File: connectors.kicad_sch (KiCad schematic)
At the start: 3 parts, among them J7 Pads for coax, J8 Relay control, J9 BNC

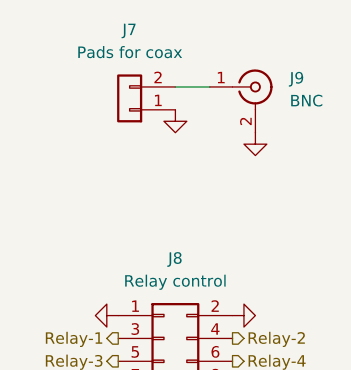
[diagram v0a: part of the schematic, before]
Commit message: changed to 1 to 6
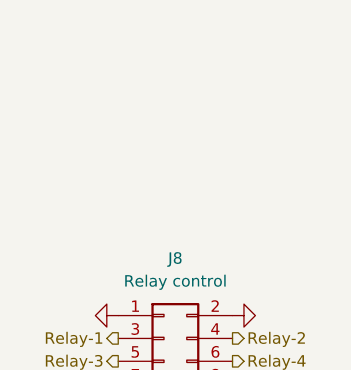
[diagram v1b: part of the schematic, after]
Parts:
- removed J7: Pads for coax, Connector_PinHeader_2.54mm:PinHeader_1x02_P2.54mm_Vertical, symbol Components:Conn_01x02
- removed J9: BNC, Components:BNC_vertical, symbol Components:BNC
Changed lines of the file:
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@@
 (kicad_sch (version 20211123) (generator eeschema)
   (paper "A4")
-  (wire (pts (xy 139.7 74.93) (xy 143.51 74.93))
-    (stroke (width 0) (type default) (color 0 0 0 0))
-  )
   (hierarchical_label "Relay-5" (shape output) (at 133.35 107.95 180)
     (effects (font (size 1.27 1.27)) (justify right))
@@
   (symbol (lib_id "power:GND") (at 146.05 100.33 90) (unit 1)
     (in_bom yes) (on_board yes) (fields_autoplaced)
-    (property "Reference" "#PWR046" (id 0) (at 152.4 100.33 0)
+    (property "Reference" "#PWR040" (id 0) (at 152.4 100.33 0)
       (effects (font (size 1.27 1.27)) hide)
     )
@@
   (symbol (lib_id "power:GND") (at 133.35 100.33 270) (mirror x) (unit 1)
     (in_bom yes) (on_board yes) (fields_autoplaced)
-    (property "Reference" "#PWR044" (id 0) (at 127 100.33 0)
+    (property "Reference" "#PWR039" (id 0) (at 127 100.33 0)
       (effects (font (size 1.27 1.27)) hide)
     )
@@
     (pin "8")
   )
-  (symbol (lib_id "Components:BNC") (at 148.59 74.93 0) (unit 1)
-    (in_bom yes) (on_board yes) (fields_autoplaced)
-    (property "Reference" "J9" (id 0) (at 152.4 73.9531 0)
-      (effects (font (size 1.27 1.27)) (justify left))
-    )
-    (property "Value" "BNC" (id 1) (at 152.4 76.4931 0)
-      (effects (font (size 1.27 1.27)) (justify left))
-    )
-    (property "Footprint" "Components:BNC_vertical" (id 2) (at 148.59 74.93 0)
-      (effects (font (size 1.27 1.27)) hide)
-    )
-    (property "Datasheet" " ~" (id 3) (at 148.59 74.93 0)
-      (effects (font (size 1.27 1.27)) hide)
-    )
-    (pin "1")
-    (pin "2")
-  )
-  (symbol (lib_id "Components:Conn_01x02") (at 134.62 77.47 180) (unit 1)
-    (in_bom yes) (on_board yes) (fields_autoplaced)
-    (property "Reference" "J7" (id 0) (at 134.62 68.58 0))
-    (property "Value" "Pads for coax" (id 1) (at 134.62 71.12 0))
-    (property "Footprint" "Connector_PinHeader_2.54mm:PinHeader_1x02_P2.54mm_Vertical" (id 2) (at 134.62 77.47 0)
-      (effects (font (size 1.27 1.27)) hide)
-    )
-    (property "Datasheet" "~" (id 3) (at 134.62 77.47 0)
-      (effects (font (size 1.27 1.27)) hide)
-    )
-    (pin "1")
-    (pin "2")
-  )
-  (symbol (lib_id "power:GND") (at 139.7 77.47 0) (unit 1)
-    (in_bom yes) (on_board yes) (fields_autoplaced)
-    (property "Reference" "#PWR045" (id 0) (at 139.7 83.82 0)
-      (effects (font (size 1.27 1.27)) hide)
-    )
-    (property "Value" "GND" (id 1) (at 139.7 82.55 0)
-      (effects (font (size 1.27 1.27)) hide)
-    )
-    (property "Footprint" "" (id 2) (at 139.7 77.47 0)
-      (effects (font (size 1.27 1.27)) hide)
-    )
-    (property "Datasheet" "" (id 3) (at 139.7 77.47 0)
-      (effects (font (size 1.27 1.27)) hide)
-    )
-    (pin "1")
-  )
-  (symbol (lib_id "power:GND") (at 148.59 80.01 0) (unit 1)
-    (in_bom yes) (on_board yes) (fields_autoplaced)
-    (property "Reference" "#PWR047" (id 0) (at 148.59 86.36 0)
-      (effects (font (size 1.27 1.27)) hide)
-    )
-    (property "Value" "GND" (id 1) (at 148.59 85.09 0)
-      (effects (font (size 1.27 1.27)) hide)
-    )
-    (property "Footprint" "" (id 2) (at 148.59 80.01 0)
-      (effects (font (size 1.27 1.27)) hide)
-    )
-    (property "Datasheet" "" (id 3) (at 148.59 80.01 0)
-      (effects (font (size 1.27 1.27)) hide)
-    )
-    (pin "1")
-  )
 )

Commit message: pcb routed and made gerbers
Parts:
- added J1: RF Conn, Components:PinHeader_2x06_P2.54mm_Horizontal, symbol Connector_Generic:Conn_02x06_Odd_Even
- renumbered J8 to J3
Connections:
- net GND: now also J1.10 (Pin_10), J1.12 (Pin_12), J1.2 (Pin_2), J1.4 (Pin_4), J1.6 (Pin_6), J1.8 (Pin_8); no longer J3.2 (Pin_2)
- net Relay-2: now also J3.5 (Pin_5); no longer J3.4 (Pin_4)
- net Relay-3: now also J3.7 (Pin_7); no longer J3.5 (Pin_5)
- net Relay-4: now also J3.8 (Pin_8); no longer J3.6 (Pin_6)
- net Relay-5: now also J3.6 (Pin_6); no longer J3.7 (Pin_7)
- net Relay-6: now also J3.4 (Pin_4); no longer J3.8 (Pin_8)
- new net +12V: J3.2 (Pin_2)
- new net RF-1: J1.1 (Pin_1)
- new net RF-2: J1.3 (Pin_3)
- new net RF-3: J1.5 (Pin_5)
- new net RF-4: J1.7 (Pin_7)
- new net RF-5: J1.9 (Pin_9)
- new net RF-6: J1.11 (Pin_11)
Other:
- note added: "2600 mils space between two j1 650 mils space between two sma on vertikal plate 3900 mils is vertical plate width 1250 mils is distance between two rf plates"
- moved on the sheet: J3
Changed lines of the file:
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@@
 (kicad_sch (version 20211123) (generator eeschema)
   (paper "A4")
-  (hierarchical_label "Relay-5" (shape output) (at 133.35 107.95 180)
+  (junction (at 147.32 57.15) (diameter 0) (color 0 0 0 0)
+  )
+  (junction (at 147.32 46.99) (diameter 0) (color 0 0 0 0)
+  )
+  (junction (at 147.32 54.61) (diameter 0) (color 0 0 0 0)
+  )
+  (junction (at 147.32 49.53) (diameter 0) (color 0 0 0 0)
+  )
+  (junction (at 147.32 52.07) (diameter 0) (color 0 0 0 0)
+  )
+  (wire (pts (xy 115.57 54.61) (xy 134.62 54.61))
+    (stroke (width 0) (type default) (color 0 0 0 0))
+  )
+  (wire (pts (xy 147.32 46.99) (xy 147.32 49.53))
+    (stroke (width 0) (type default) (color 0 0 0 0))
+  )
+  (wire (pts (xy 147.32 44.45) (xy 147.32 46.99))
+    (stroke (width 0) (type default) (color 0 0 0 0))
+  )
+  (wire (pts (xy 147.32 52.07) (xy 147.32 54.61))
+    (stroke (width 0) (type default) (color 0 0 0 0))
+  )
+  (wire (pts (xy 147.32 49.53) (xy 147.32 52.07))
+    (stroke (width 0) (type default) (color 0 0 0 0))
+  )
+  (wire (pts (xy 115.57 46.99) (xy 134.62 46.99))
+    (stroke (width 0) (type default) (color 0 0 0 0))
+  )
+  (wire (pts (xy 115.57 52.07) (xy 134.62 52.07))
+    (stroke (width 0) (type default) (color 0 0 0 0))
+  )
+  (wire (pts (xy 115.57 57.15) (xy 134.62 57.15))
+    (stroke (width 0) (type default) (color 0 0 0 0))
+  )
+  (wire (pts (xy 115.57 44.45) (xy 134.62 44.45))
+    (stroke (width 0) (type default) (color 0 0 0 0))
+  )
+  (wire (pts (xy 147.32 57.15) (xy 147.32 59.69))
+    (stroke (width 0) (type default) (color 0 0 0 0))
+  )
+  (wire (pts (xy 148.59 111.76) (xy 146.05 111.76))
+    (stroke (width 0) (type default) (color 0 0 0 0))
+  )
+  (wire (pts (xy 115.57 49.53) (xy 134.62 49.53))
+    (stroke (width 0) (type default) (color 0 0 0 0))
+  )
+  (wire (pts (xy 147.32 54.61) (xy 147.32 57.15))
+    (stroke (width 0) (type default) (color 0 0 0 0))
+  )
+  (text "2600 mils space between two j1\n 650 mils space between two sma on vertikal plate\n3900 mils is vertical plate width\n1250 mils is distance between two rf plates"
+    (at 153.67 52.07 0)
+    (effects (font (size 1.27 1.27)) (justify left bottom))
+  )
+  (hierarchical_label "RF-3" (shape output) (at 115.57 49.53 180)
     (effects (font (size 1.27 1.27)) (justify right))
   )
-  (hierarchical_label "Relay-6" (shape output) (at 146.05 107.95 0)
+  (hierarchical_label "Relay-5" (shape output) (at 146.05 116.84 0)
     (effects (font (size 1.27 1.27)) (justify left))
   )
-  (hierarchical_label "Relay-2" (shape output) (at 146.05 102.87 0)
+  (hierarchical_label "Relay-6" (shape output) (at 146.05 114.3 0)
     (effects (font (size 1.27 1.27)) (justify left))
   )
-  (hierarchical_label "Relay-1" (shape output) (at 133.35 102.87 180)
+  (hierarchical_label "RF-6" (shape output) (at 115.57 57.15 180)
     (effects (font (size 1.27 1.27)) (justify right))
   )
-  (hierarchical_label "Relay-3" (shape output) (at 133.35 105.41 180)
+  (hierarchical_label "Relay-2" (shape output) (at 133.35 116.84 180)
     (effects (font (size 1.27 1.27)) (justify right))
   )
-  (hierarchical_label "Relay-4" (shape output) (at 146.05 105.41 0)
+  (hierarchical_label "RF-1" (shape output) (at 115.57 44.45 180)
+    (effects (font (size 1.27 1.27)) (justify right))
+  )
+  (hierarchical_label "RF-2" (shape output) (at 115.57 46.99 180)
+    (effects (font (size 1.27 1.27)) (justify right))
+  )
+  (hierarchical_label "Relay-1" (shape output) (at 133.35 114.3 180)
+    (effects (font (size 1.27 1.27)) (justify right))
+  )
+  (hierarchical_label "RF-5" (shape output) (at 115.57 54.61 180)
+    (effects (font (size 1.27 1.27)) (justify right))
+  )
+  (hierarchical_label "Relay-3" (shape output) (at 133.35 119.38 180)
+    (effects (font (size 1.27 1.27)) (justify right))
+  )
+  (hierarchical_label "Relay-4" (shape output) (at 146.05 119.38 0)
     (effects (font (size 1.27 1.27)) (justify left))
   )
-  (symbol (lib_id "power:GND") (at 146.05 100.33 90) (unit 1)
+  (hierarchical_label "RF-4" (shape output) (at 115.57 52.07 180)
+    (effects (font (size 1.27 1.27)) (justify right))
+  )
+  (symbol (lib_id "power:GND") (at 133.35 111.76 270) (mirror x) (unit 1)
     (in_bom yes) (on_board yes) (fields_autoplaced)
-    (property "Reference" "#PWR040" (id 0) (at 152.4 100.33 0)
+    (property "Reference" "#PWR039" (id 0) (at 127 111.76 0)
       (effects (font (size 1.27 1.27)) hide)
     )
-    (property "Value" "GND" (id 1) (at 151.13 100.33 0)
+    (property "Value" "GND" (id 1) (at 128.27 111.76 0)
       (effects (font (size 1.27 1.27)) hide)
     )
-    (property "Footprint" "" (id 2) (at 146.05 100.33 0)
+    (property "Footprint" "" (id 2) (at 133.35 111.76 0)
       (effects (font (size 1.27 1.27)) hide)
     )
-    (property "Datasheet" "" (id 3) (at 146.05 100.33 0)
+    (property "Datasheet" "" (id 3) (at 133.35 111.76 0)
       (effects (font (size 1.27 1.27)) hide)
     )
     (pin "1")
   )
-  (symbol (lib_id "power:GND") (at 133.35 100.33 270) (mirror x) (unit 1)
+  (symbol (lib_id "Components:Conn_02x04_Odd_Even") (at 138.43 114.3 0) (unit 1)
     (in_bom yes) (on_board yes) (fields_autoplaced)
-    (property "Reference" "#PWR039" (id 0) (at 127 100.33 0)
+    (property "Reference" "J3" (id 0) (at 139.7 105.41 0))
+    (property "Value" "Relay control" (id 1) (at 139.7 107.95 0))
+    (property "Footprint" "Connector_PinHeader_2.54mm:PinHeader_2x04_P2.54mm_Vertical" (id 2) (at 138.43 114.3 0)
       (effects (font (size 1.27 1.27)) hide)
     )
-    (property "Value" "GND" (id 1) (at 128.27 100.33 0)
-      (effects (font (size 1.27 1.27)) hide)
-    )
-    (property "Footprint" "" (id 2) (at 133.35 100.33 0)
-      (effects (font (size 1.27 1.27)) hide)
-    )
-    (property "Datasheet" "" (id 3) (at 133.35 100.33 0)
-      (effects (font (size 1.27 1.27)) hide)
-    )
-    (pin "1")
-  )
-  (symbol (lib_id "Components:Conn_02x04_Odd_Even") (at 138.43 102.87 0) (unit 1)
-    (in_bom yes) (on_board yes) (fields_autoplaced)
-    (property "Reference" "J8" (id 0) (at 139.7 93.98 0))
-    (property "Value" "Relay control" (id 1) (at 139.7 96.52 0))
-    (property "Footprint" "Connector_PinHeader_2.54mm:PinHeader_2x04_P2.54mm_Vertical" (id 2) (at 138.43 102.87 0)
-      (effects (font (size 1.27 1.27)) hide)
-    )
-    (property "Datasheet" "~" (id 3) (at 138.43 102.87 0)
+    (property "Datasheet" "~" (id 3) (at 138.43 114.3 0)
       (effects (font (size 1.27 1.27)) hide)
     )
@@
     (pin "8")
   )
+  (symbol (lib_id "power:+12V") (at 148.59 111.76 0) (unit 1)
+    (in_bom yes) (on_board yes) (fields_autoplaced)
+    (property "Reference" "#PWR?" (id 0) (at 148.59 115.57 0)
+      (effects (font (size 1.27 1.27)) hide)
+    )
+    (property "Value" "+12V" (id 1) (at 148.59 106.68 0))
+    (property "Footprint" "" (id 2) (at 148.59 111.76 0)
+      (effects (font (size 1.27 1.27)) hide)
+    )
+    (property "Datasheet" "" (id 3) (at 148.59 111.76 0)
+      (effects (font (size 1.27 1.27)) hide)
+    )
+    (pin "1")
+  )
+  (symbol (lib_id "power:GND") (at 147.32 59.69 0) (mirror y) (unit 1)
+    (in_bom yes) (on_board yes) (fields_autoplaced)
+    (property "Reference" "#PWR012" (id 0) (at 147.32 66.04 0)
+      (effects (font (size 1.27 1.27)) hide)
+    )
+    (property "Value" "GND" (id 1) (at 147.32 64.77 0)
+      (effects (font (size 1.27 1.27)) hide)
+    )
+    (property "Footprint" "" (id 2) (at 147.32 59.69 0)
+      (effects (font (size 1.27 1.27)) hide)
+    )
+    (property "Datasheet" "" (id 3) (at 147.32 59.69 0)
+      (effects (font (size 1.27 1.27)) hide)
+    )
+    (pin "1")
+  )
+  (symbol (lib_id "Connector_Generic:Conn_02x06_Odd_Even") (at 139.7 49.53 0) (unit 1)
+    (in_bom yes) (on_board yes) (fields_autoplaced)
+    (property "Reference" "J1" (id 0) (at 140.97 38.1 0))
+    (property "Value" "RF Conn" (id 1) (at 140.97 40.64 0))
+    (property "Footprint" "Components:PinHeader_2x06_P2.54mm_Horizontal" (id 2) (at 139.7 49.53 0)
+      (effects (font (size 1.27 1.27)) hide)
+    )
+    (property "Datasheet" "~" (id 3) (at 139.7 49.53 0)
+      (effects (font (size 1.27 1.27)) hide)
+    )
+    (pin "1")
+    (pin "10")
+    (pin "11")
+    (pin "12")
+    (pin "2")
+    (pin "3")
+    (pin "4")
+    (pin "5")
+    (pin "6")
+    (pin "7")
+    (pin "8")
+    (pin "9")
+  )
 )

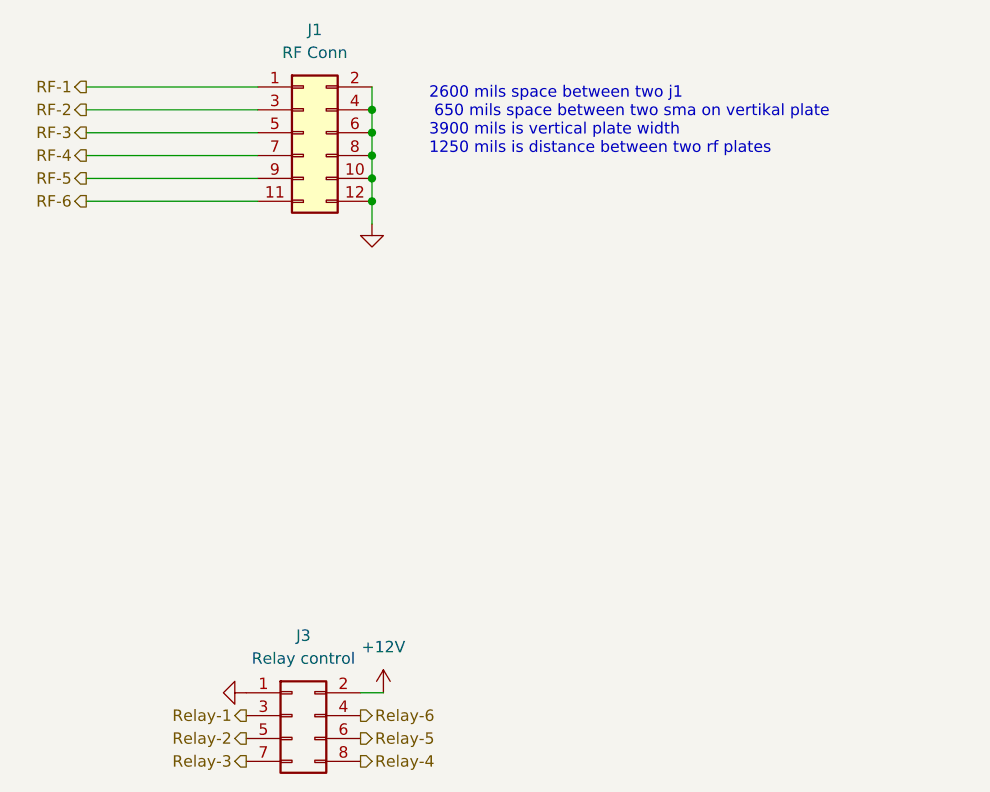
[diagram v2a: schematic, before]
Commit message: add block capacitor
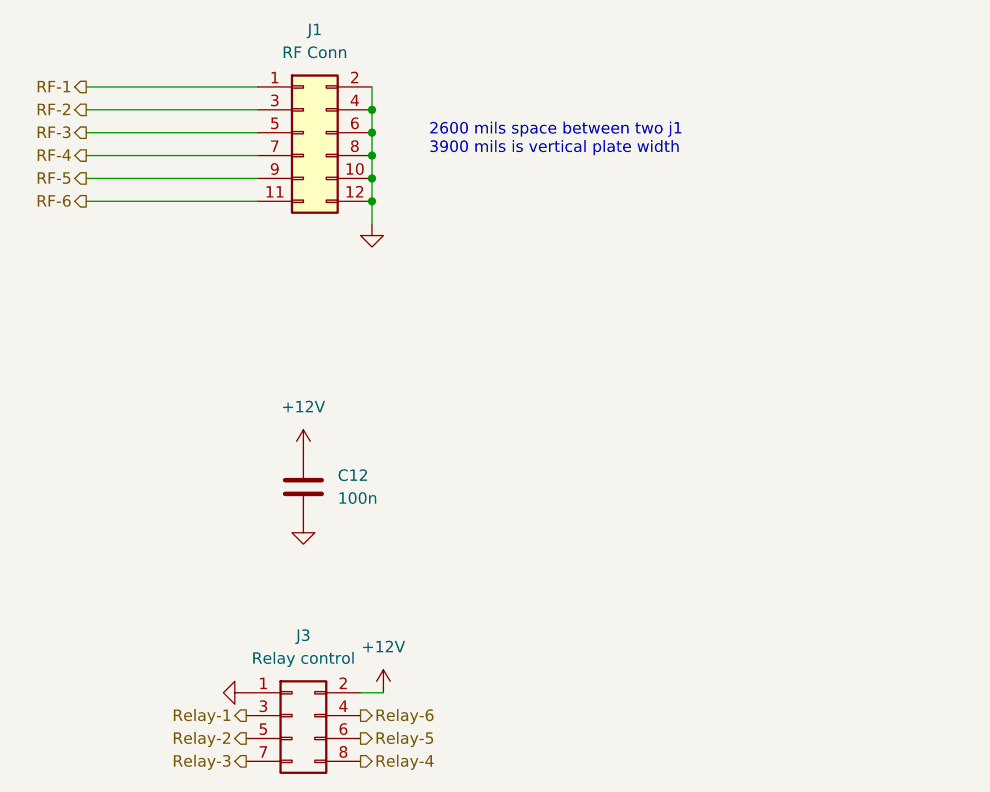
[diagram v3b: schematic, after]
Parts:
- added C12: 100n, Capacitor_SMD:C_0603_1608Metric_Pad1.08x0.95mm_HandSolder, symbol Device:C
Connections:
- net +12V: now also C12.1
- net GND: now also C12.2
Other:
- note added: "2600 mils space between two j1 3900 mils is vertical plate width"
- note removed: "2600 mils space between two j1 650 mils space between two sma on vertikal plate 3900 mils is vertical plate width 1250 mils is distance between two rf plates"
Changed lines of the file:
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@@
     (stroke (width 0) (type default) (color 0 0 0 0))
   )
-  (text "2600 mils space between two j1\n 650 mils space between two sma on vertikal plate\n3900 mils is vertical plate width\n1250 mils is distance between two rf plates"
+  (text "2600 mils space between two j1\n3900 mils is vertical plate width\n"
     (at 153.67 52.07 0)
     (effects (font (size 1.27 1.27)) (justify left bottom))
@@
   (symbol (lib_id "power:+12V") (at 148.59 111.76 0) (unit 1)
     (in_bom yes) (on_board yes) (fields_autoplaced)
-    (property "Reference" "#PWR?" (id 0) (at 148.59 115.57 0)
+    (property "Reference" "#PWR036" (id 0) (at 148.59 115.57 0)
       (effects (font (size 1.27 1.27)) hide)
     )
@@
       (effects (font (size 1.27 1.27)) hide)
     )
+    (pin "1")
+  )
+  (symbol (lib_id "power:+12V") (at 139.7 85.09 0) (unit 1)
+    (in_bom yes) (on_board yes) (fields_autoplaced)
+    (property "Reference" "#PWR026" (id 0) (at 139.7 88.9 0)
+      (effects (font (size 1.27 1.27)) hide)
+    )
+    (property "Value" "+12V" (id 1) (at 139.7 80.01 0))
+    (property "Footprint" "" (id 2) (at 139.7 85.09 0)
+      (effects (font (size 1.27 1.27)) hide)
+    )
+    (property "Datasheet" "" (id 3) (at 139.7 85.09 0)
+      (effects (font (size 1.27 1.27)) hide)
+    )
+    (pin "1")
+  )
+  (symbol (lib_id "Device:C") (at 139.7 88.9 0) (unit 1)
+    (in_bom yes) (on_board yes) (fields_autoplaced)
+    (property "Reference" "C12" (id 0) (at 143.51 87.6299 0)
+      (effects (font (size 1.27 1.27)) (justify left))
+    )
+    (property "Value" "100n" (id 1) (at 143.51 90.1699 0)
+      (effects (font (size 1.27 1.27)) (justify left))
+    )
+    (property "Footprint" "Capacitor_SMD:C_0603_1608Metric_Pad1.08x0.95mm_HandSolder" (id 2) (at 140.6652 92.71 0)
+      (effects (font (size 1.27 1.27)) hide)
+    )
+    (property "Datasheet" "~" (id 3) (at 139.7 88.9 0)
+      (effects (font (size 1.27 1.27)) hide)
+    )
+    (pin "1")
+    (pin "2")
+  )
+  (symbol (lib_id "power:GND") (at 139.7 92.71 0) (mirror y) (unit 1)
+    (in_bom yes) (on_board yes) (fields_autoplaced)
+    (property "Reference" "#PWR031" (id 0) (at 139.7 99.06 0)
+      (effects (font (size 1.27 1.27)) hide)
+    )
+    (property "Value" "GND" (id 1) (at 139.7 97.79 0)
+      (effects (font (size 1.27 1.27)) hide)
+    )
+    (property "Footprint" "" (id 2) (at 139.7 92.71 0)
+      (effects (font (size 1.27 1.27)) hide)
+    )
+    (property "Datasheet" "" (id 3) (at 139.7 92.71 0)
+      (effects (font (size 1.27 1.27)) hide)
+    )

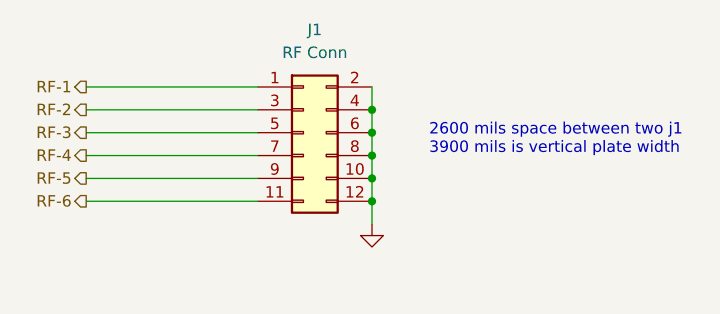
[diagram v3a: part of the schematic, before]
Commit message: changed footprint for 2-way splitter transformer
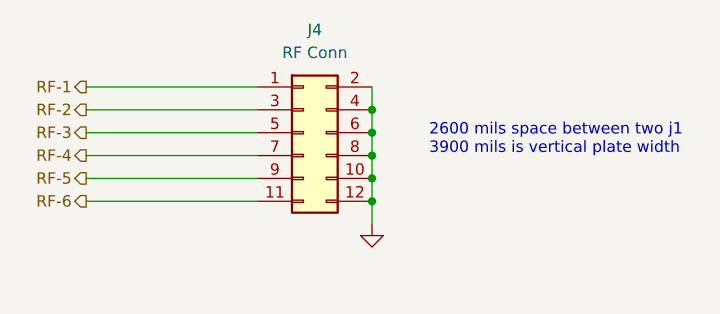
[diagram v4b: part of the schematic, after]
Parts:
- renumbered J1 to J4
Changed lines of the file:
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@@
   (symbol (lib_id "power:GND") (at 133.35 111.76 270) (mirror x) (unit 1)
     (in_bom yes) (on_board yes) (fields_autoplaced)
-    (property "Reference" "#PWR039" (id 0) (at 127 111.76 0)
+    (property "Reference" "#PWR0133" (id 0) (at 127 111.76 0)
       (effects (font (size 1.27 1.27)) hide)
     )
@@
   (symbol (lib_id "power:+12V") (at 148.59 111.76 0) (unit 1)
     (in_bom yes) (on_board yes) (fields_autoplaced)
-    (property "Reference" "#PWR036" (id 0) (at 148.59 115.57 0)
+    (property "Reference" "#PWR0132" (id 0) (at 148.59 115.57 0)
       (effects (font (size 1.27 1.27)) hide)
     )
@@
   (symbol (lib_id "power:GND") (at 147.32 59.69 0) (mirror y) (unit 1)
     (in_bom yes) (on_board yes) (fields_autoplaced)
-    (property "Reference" "#PWR012" (id 0) (at 147.32 66.04 0)
+    (property "Reference" "#PWR0129" (id 0) (at 147.32 66.04 0)
       (effects (font (size 1.27 1.27)) hide)
     )
@@
   (symbol (lib_id "power:+12V") (at 139.7 85.09 0) (unit 1)
     (in_bom yes) (on_board yes) (fields_autoplaced)
-    (property "Reference" "#PWR026" (id 0) (at 139.7 88.9 0)
+    (property "Reference" "#PWR0130" (id 0) (at 139.7 88.9 0)
       (effects (font (size 1.27 1.27)) hide)
     )
@@
   (symbol (lib_id "power:GND") (at 139.7 92.71 0) (mirror y) (unit 1)
     (in_bom yes) (on_board yes) (fields_autoplaced)
-    (property "Reference" "#PWR031" (id 0) (at 139.7 99.06 0)
+    (property "Reference" "#PWR0131" (id 0) (at 139.7 99.06 0)
       (effects (font (size 1.27 1.27)) hide)
     )
@@
   (symbol (lib_id "Connector_Generic:Conn_02x06_Odd_Even") (at 139.7 49.53 0) (unit 1)
     (in_bom yes) (on_board yes) (fields_autoplaced)
-    (property "Reference" "J1" (id 0) (at 140.97 38.1 0))
+    (property "Reference" "J4" (id 0) (at 140.97 38.1 0))
     (property "Value" "RF Conn" (id 1) (at 140.97 40.64 0))
     (property "Footprint" "Components:PinHeader_2x06_P2.54mm_Horizontal" (id 2) (at 139.7 49.53 0)
